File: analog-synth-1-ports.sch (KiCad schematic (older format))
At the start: 16 parts, among them J1 Conn_02x08_Odd_Even, J2 PJ301M-12, J3 PJ301M-12, J4 PJ301M-12, J5 PJ301M-12, Q1 2N3904, Q2 2N3904, U1 TL084, U2 TL084

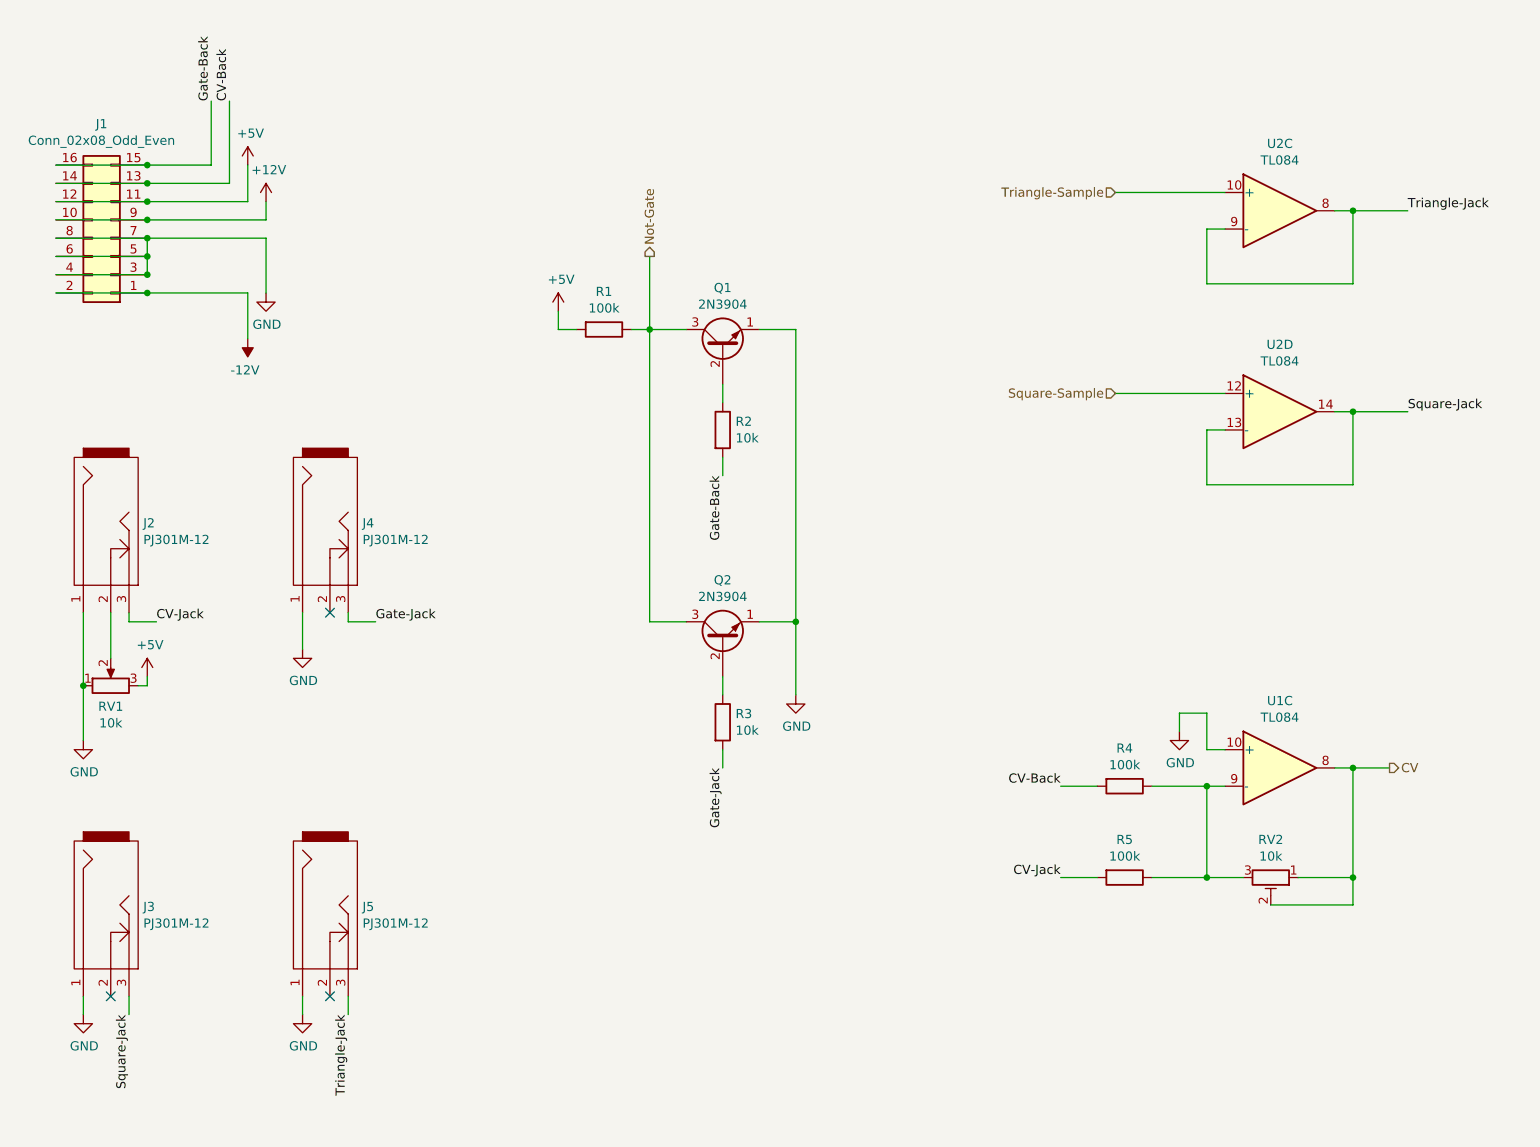
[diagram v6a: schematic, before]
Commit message: Add ATtiny85 overdrive protection, fix #5
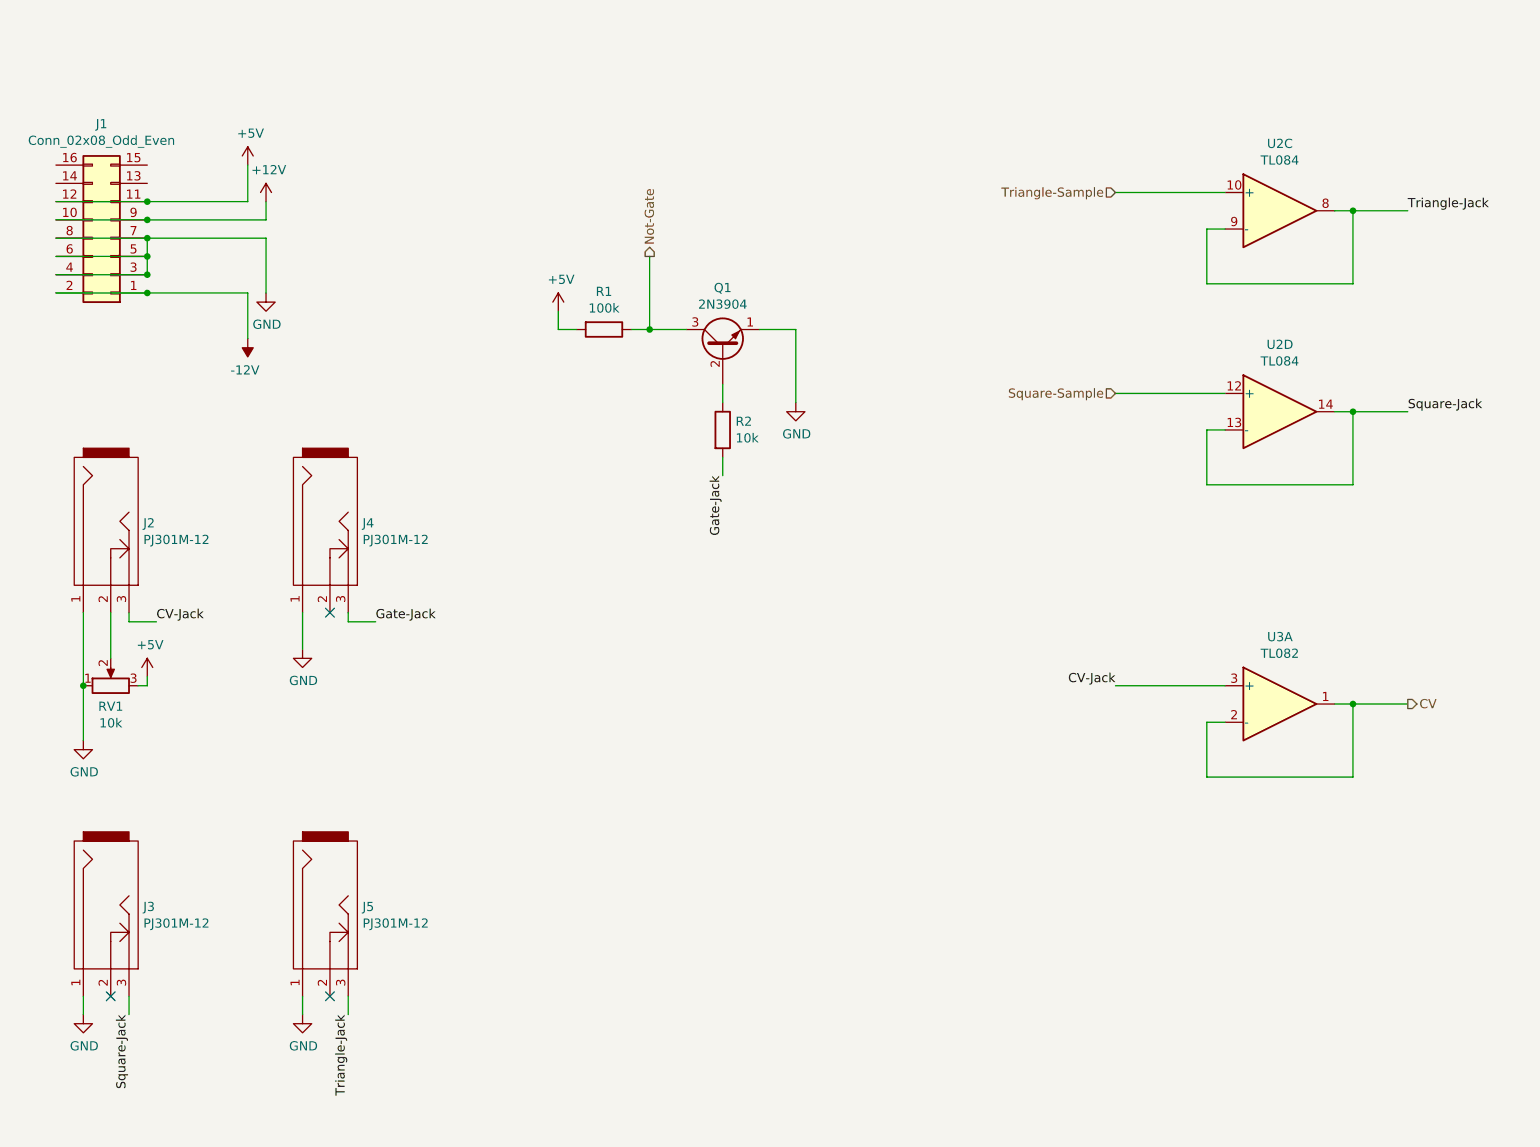
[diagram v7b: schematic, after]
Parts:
- removed Q1: 2N3904, Package_TO_SOT_THT:TO-92_Inline, symbol Transistor_BJT:2N3904
- removed R2: 10k, symbol Device:R
- removed R4, R5: 100k, symbol Device:R
- removed RV2: 10k, symbol Device:R_POT_TRIM
- removed U1: TL084, symbol Amplifier_Operational:TL084
- added U3: TL082, symbol Amplifier_Operational:TL082
- renumbered Q2 to Q1, R3 to R2
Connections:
- net CV: now also U3.1, U3.2 (-)
- net CV-Jack: now also U3.3 (+)
- net CV-Back: no longer names the net of J1.13 (Pin_13)
- net CV-Back: no longer J1.14 (Pin_14)
- net Gate-Back: no longer names the net of J1.15 (Pin_15)
- net Gate-Back: no longer J1.16 (Pin_16)
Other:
- moved on the sheet: Q1, R2
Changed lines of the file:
@@
 	1750 1900 2250 1900
-Wire Wire Line
-	1750 1800 2250 1800
-Wire Wire Line
-	1750 1700 2250 1700
 Wire Wire Line
 	2250 2100 2250 2200
@@
 NoConn ~ 2050 6250
 $Comp
-L power:GND #PWR018
+L power:GND #PWR021
 U 1 1 5C877B99
 P 3100 6350
-F 0 "#PWR018" H 3100 6100 50  0001 C CNN
+F 0 "#PWR021" H 3100 6100 50  0001 C CNN
 F 1 "GND" H 3105 6177 50  0000 C CNN
 F 2 "" H 3100 6350 50  0001 C CNN
@@
 	9150 3050 8850 3050
 Connection ~ 8850 3050
-$Comp
-L Amplifier_Operational:TL084 U1
-U 3 1 5C87D386
-P 8450 5000
-F 0 "U1" H 8450 5367 50  0000 C CNN
-F 1 "TL084" H 8450 5276 50  0000 C CNN
-F 2 "" H 8400 5100 50  0001 C CNN
-F 3 "http://www.ti.com/lit/ds/symlink/tl081.pdf" H 8500 5200 50  0001 C CNN
-	3    8450 5000
-	1    0    0    -1
-$EndComp
-$Comp
-L Device:R_POT_TRIM RV2
-U 1 1 5C87DFED
-P 8400 5600
-F 0 "RV2" V 8193 5600 50  0000 C CNN
-F 1 "10k" V 8284 5600 50  0000 C CNN
-F 2 "" H 8400 5600 50  0001 C CNN
-F 3 "~" H 8400 5600 50  0001 C CNN
-	1    8400 5600
-	0    1    1    0
-$EndComp
-Wire Wire Line
-	8550 5600 8850 5600
-Wire Wire Line
-	8850 5600 8850 5000
-Wire Wire Line
-	8850 5000 8750 5000
-Wire Wire Line
-	8250 5600 8050 5600
-Wire Wire Line
-	8050 5600 8050 5100
-Wire Wire Line
-	8050 5100 8150 5100
-Wire Wire Line
-	8400 5750 8850 5750
-Wire Wire Line
-	8850 5750 8850 5600
-Connection ~ 8850 5600
-$Comp
-L power:GND #PWR021
-U 1 1 5C880099
-P 7900 4800
-F 0 "#PWR021" H 7900 4550 50  0001 C CNN
-F 1 "GND" H 7905 4627 50  0000 C CNN
-F 2 "" H 7900 4800 50  0001 C CNN
-F 3 "" H 7900 4800 50  0001 C CNN
-	1    7900 4800
-	1    0    0    -1
-$EndComp
-Wire Wire Line
-	8150 4900 8050 4900
-Wire Wire Line
-	8050 4900 8050 4700
-Wire Wire Line
-	8050 4700 7900 4700
-Wire Wire Line
-	7900 4700 7900 4800
-$Comp
-L Device:R R4
-U 1 1 5C880E42
-P 7600 5100
-F 0 "R4" V 7393 5100 50  0000 C CNN
-F 1 "100k" V 7484 5100 50  0000 C CNN
-F 2 "" V 7530 5100 50  0001 C CNN
-F 3 "~" H 7600 5100 50  0001 C CNN
-	1    7600 5100
-	0    1    1    0
-$EndComp
-$Comp
-L Device:R R5
-U 1 1 5C880EB3
-P 7600 5600
-F 0 "R5" V 7393 5600 50  0000 C CNN
-F 1 "100k" V 7484 5600 50  0000 C CNN
-F 2 "" V 7530 5600 50  0001 C CNN
-F 3 "~" H 7600 5600 50  0001 C CNN
-	1    7600 5600
-	0    1    1    0
-$EndComp
-Wire Wire Line
-	7750 5100 8050 5100
-Connection ~ 8050 5100
-Wire Wire Line
-	7750 5600 8050 5600
-Connection ~ 8050 5600
-Wire Wire Line
-	7250 5100 7450 5100
-Wire Wire Line
-	7250 5600 7450 5600
-Wire Wire Line
-	9050 5000 8850 5000
-Connection ~ 8850 5000
 Wire Wire Line
 	1900 4550 1900 4850
@@
 $EndComp
 $Comp
-L power:GND #PWR011
+L power:GND #PWR014
 U 1 1 5C876B03
 P 1900 6350
-F 0 "#PWR011" H 1900 6100 50  0001 C CNN
+F 0 "#PWR014" H 1900 6100 50  0001 C CNN
 F 1 "GND" H 1905 6177 50  0000 C CNN
 F 2 "" H 1900 6350 50  0001 C CNN
@@
 $EndComp
 $Comp
-L power:GND #PWR017
+L power:GND #PWR020
 U 1 1 5C875167
 P 3100 4350
-F 0 "#PWR017" H 3100 4100 50  0001 C CNN
+F 0 "#PWR020" H 3100 4100 50  0001 C CNN
 F 1 "GND" H 3105 4177 50  0000 C CNN
 F 2 "" H 3100 4350 50  0001 C CNN
@@
 $EndComp
 $Comp
-L power:GND #PWR010
+L power:GND #PWR013
 U 1 1 5C873F44
 P 1900 4850
-F 0 "#PWR010" H 1900 4600 50  0001 C CNN
+F 0 "#PWR013" H 1900 4600 50  0001 C CNN
 F 1 "GND" H 1905 4677 50  0000 C CNN
 F 2 "" H 1900 4850 50  0001 C CNN
@@
 $EndComp
 $Comp
-L power:+5V #PWR012
+L power:+5V #PWR015
 U 1 1 5C87478A
 P 2250 4500
-F 0 "#PWR012" H 2250 4350 50  0001 C CNN
+F 0 "#PWR015" H 2250 4350 50  0001 C CNN
 F 1 "+5V" H 2265 4673 50  0000 C CNN
 F 2 "" H 2250 4500 50  0001 C CNN
@@
 Wire Wire Line
 	2800 1700 2800 1900
-Connection ~ 2250 1800
-Wire Wire Line
-	2700 1800 2250 1800
-Connection ~ 2250 1700
-Wire Wire Line
-	2600 1700 2250 1700
-Wire Wire Line
-	2700 1350 2700 1800
-Wire Wire Line
-	2600 1350 2600 1700
-$Comp
-L power:-12V #PWR014
+$Comp
+L power:-12V #PWR017
 U 1 1 5C85BF08
 P 2800 2650
-F 0 "#PWR014" H 2800 2750 50  0001 C CNN
+F 0 "#PWR017" H 2800 2750 50  0001 C CNN
 F 1 "-12V" H 2815 2823 50  0000 C CNN
 F 2 "" H 2800 2650 50  0001 C CNN
@@
 $EndComp
 $Comp
-L power:GND #PWR016
+L power:GND #PWR019
 U 1 1 5C85BD09
 P 2900 2400
-F 0 "#PWR016" H 2900 2150 50  0001 C CNN
+F 0 "#PWR019" H 2900 2150 50  0001 C CNN
 F 1 "GND" H 2905 2227 50  0000 C CNN
 F 2 "" H 2900 2400 50  0001 C CNN
@@
 $EndComp
 $Comp
-L power:+12V #PWR015
+L power:+12V #PWR018
 U 1 1 5C85B8F4
 P 2900 1900
-F 0 "#PWR015" H 2900 1750 50  0001 C CNN
+F 0 "#PWR018" H 2900 1750 50  0001 C CNN
 F 1 "+12V" H 2915 2073 50  0000 C CNN
 F 2 "" H 2900 1900 50  0001 C CNN
@@
 $EndComp
 $Comp
-L power:+5V #PWR013
+L power:+5V #PWR016
 U 1 1 5C85B77F
 P 2800 1700
-F 0 "#PWR013" H 2800 1550 50  0001 C CNN
+F 0 "#PWR016" H 2800 1550 50  0001 C CNN
 F 1 "+5V" H 2815 1873 50  0000 C CNN
 F 2 "" H 2800 1700 50  0001 C CNN
@@
 Text Label 3500 4200 0    50   ~ 0
 Gate-Jack
-Text Label 2700 1350 1    50   ~ 0
-CV-Back
-Text Label 2600 1350 1    50   ~ 0
-Gate-Back
 Text Label 3350 6350 3    50   ~ 0
 Triangle-Jack
 Text Label 2150 6350 3    50   ~ 0
 Square-Jack
-Text Label 7250 5100 2    50   ~ 0
-CV-Back
-Text Label 7250 5600 2    50   ~ 0
-CV-Jack
-Text HLabel 9050 5000 2    50   Output ~ 0
-CV
 Text HLabel 7550 1850 0    50   Input ~ 0
 Triangle-Sample
@@
 Square-Jack
 $Comp
-L Transistor_BJT:2N3904 Q2
+L Transistor_BJT:2N3904 Q1
 U 1 1 5C88672F
-P 5400 4300
-F 0 "Q2" V 5728 4300 50  0000 C CNN
-F 1 "2N3904" V 5637 4300 50  0000 C CNN
-F 2 "Package_TO_SOT_THT:TO-92_Inline" H 5600 4225 50  0001 L CIN
-F 3 "https://www.fairchildsemi.com/datasheets/2N/2N3904.pdf" H 5400 4300 50  0001 L CNN
-	1    5400 4300
-	0    -1   -1   0
-$EndComp
-$Comp
-L Transistor_BJT:2N3904 Q1
-U 1 1 5C8869D4
 P 5400 2700
 F 0 "Q1" V 5728 2700 50  0000 C CNN
@@
 $Comp
 L Device:R R2
-U 1 1 5C888524
+U 1 1 5C888587
 P 5400 3150
 F 0 "R2" H 5470 3196 50  0000 L CNN
@@
 	1    0    0    -1
 $EndComp
-$Comp
-L Device:R R3
-U 1 1 5C888587
-P 5400 4750
-F 0 "R3" H 5470 4796 50  0000 L CNN
-F 1 "10k" H 5470 4705 50  0000 L CNN
-F 2 "" V 5330 4750 50  0001 C CNN
-F 3 "~" H 5400 4750 50  0001 C CNN
-	1    5400 4750
-	1    0    0    -1
-$EndComp
 Wire Wire Line
 	5400 2900 5400 3000
-Wire Wire Line
-	5400 4500 5400 4600
 Text Label 5400 3400 3    50   ~ 0
-Gate-Back
+Gate-Jack
 Wire Wire Line
 	5400 3300 5400 3400
-Text Label 5400 5000 3    50   ~ 0
-Gate-Jack
-Wire Wire Line
-	5400 4900 5400 5000
-$Comp
-L power:GND #PWR020
+$Comp
+L power:GND #PWR023
 U 1 1 5C88EC7D
-P 5800 4600
-F 0 "#PWR020" H 5800 4350 50  0001 C CNN
-F 1 "GND" H 5805 4427 50  0000 C CNN
-F 2 "" H 5800 4600 50  0001 C CNN
-F 3 "" H 5800 4600 50  0001 C CNN
-	1    5800 4600
-	1    0    0    -1
-$EndComp
-Wire Wire Line
-	5800 4600 5800 4200
-Wire Wire Line
-	5800 4200 5600 4200
-Wire Wire Line
-	5800 4200 5800 2600
+P 5800 3000
+F 0 "#PWR023" H 5800 2750 50  0001 C CNN
+F 1 "GND" H 5805 2827 50  0000 C CNN
+F 2 "" H 5800 3000 50  0001 C CNN
+F 3 "" H 5800 3000 50  0001 C CNN
+	1    5800 3000
+	1    0    0    -1
+$EndComp
+Wire Wire Line
+	5800 3000 5800 2600
 Wire Wire Line
 	5800 2600 5600 2600
-Connection ~ 5800 4200
 Text HLabel 5000 2200 1    50   Output ~ 0
 Not-Gate
@@
 Wire Wire Line
 	5000 2600 5200 2600
-Wire Wire Line
-	5000 2600 5000 4200
-Wire Wire Line
-	5000 4200 5200 4200
-Connection ~ 5000 2600
 $Comp
 L Device:R R1
@@
 $EndComp
 $Comp
-L power:+5V #PWR019
+L power:+5V #PWR022
 U 1 1 5C894E75
 P 4500 2500
-F 0 "#PWR019" H 4500 2350 50  0001 C CNN
+F 0 "#PWR022" H 4500 2350 50  0001 C CNN
 F 1 "+5V" H 4515 2673 50  0000 C CNN
 F 2 "" H 4500 2500 50  0001 C CNN
@@
 Wire Wire Line
 	4900 2600 5000 2600
+Connection ~ 5000 2600
+$Comp
+L Amplifier_Operational:TL082 U3
+U 1 1 5CA17F7A
+P 8450 4650
+F 0 "U3" H 8450 5017 50  0000 C CNN
+F 1 "TL082" H 8450 4926 50  0000 C CNN
+F 2 "" H 8450 4650 50  0001 C CNN
+F 3 "http://www.ti.com/lit/ds/symlink/tl081.pdf" H 8450 4650 50  0001 C CNN
+	1    8450 4650
+	1    0    0    -1
+$EndComp
+Text Label 7550 4550 2    50   ~ 0
+CV-Jack
+Wire Wire Line
+	7550 4550 8150 4550
+Text HLabel 9150 4650 2    50   Output ~ 0
+CV
+Wire Wire Line
+	9150 4650 8850 4650
+Wire Wire Line
+	8850 4650 8850 5050
+Wire Wire Line
+	8850 5050 8050 5050
+Wire Wire Line
+	8050 5050 8050 4750
+Wire Wire Line
+	8050 4750 8150 4750
+Connection ~ 8850 4650
+Wire Wire Line
+	8850 4650 8750 4650
 $EndSCHEMATC
